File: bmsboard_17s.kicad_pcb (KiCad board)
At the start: 2 copper layers, 141 parts, among them Q1 Q_NMOS_GDS, Q10 Q_NMOS_GDS, Q11 Q_NMOS_GDS, Q12 Q_PMOS_GDS, Q13 Q_NMOS_GDS, Q14 Q_NMOS_GDS, Q15 Q_NMOS_GDS, Q16 Q_NMOS_GDS, Q17 Q_NMOS_GDS, Q18 Q_NMOS_GDS, Q19 Q_NMOS_GDS, Q2 Q_NMOS_GDS, Q20 Q_NMOS_GDS, Q21 Q_NPN_BCE, Q3 Q_NMOS_GDS, Q4 Q_NMOS_GDS, Q5 Q_NMOS_GDS, Q6 Q_NMOS_GDS, Q7 Q_NMOS_GDS, Q8 Q_NMOS_GDS, Q9 Q_NMOS_GDS, U1 PB7170

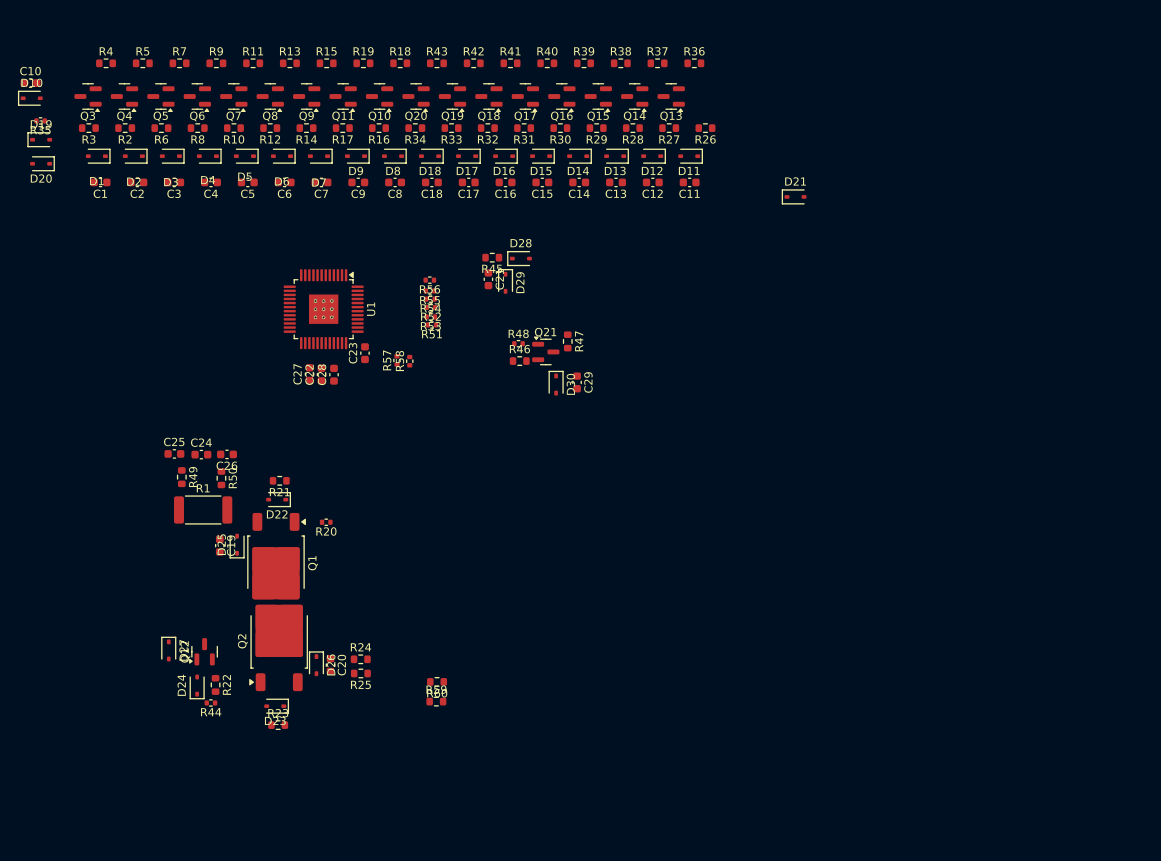
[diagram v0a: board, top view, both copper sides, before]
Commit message: 重新分配位号，使电压采样电路的位号连续
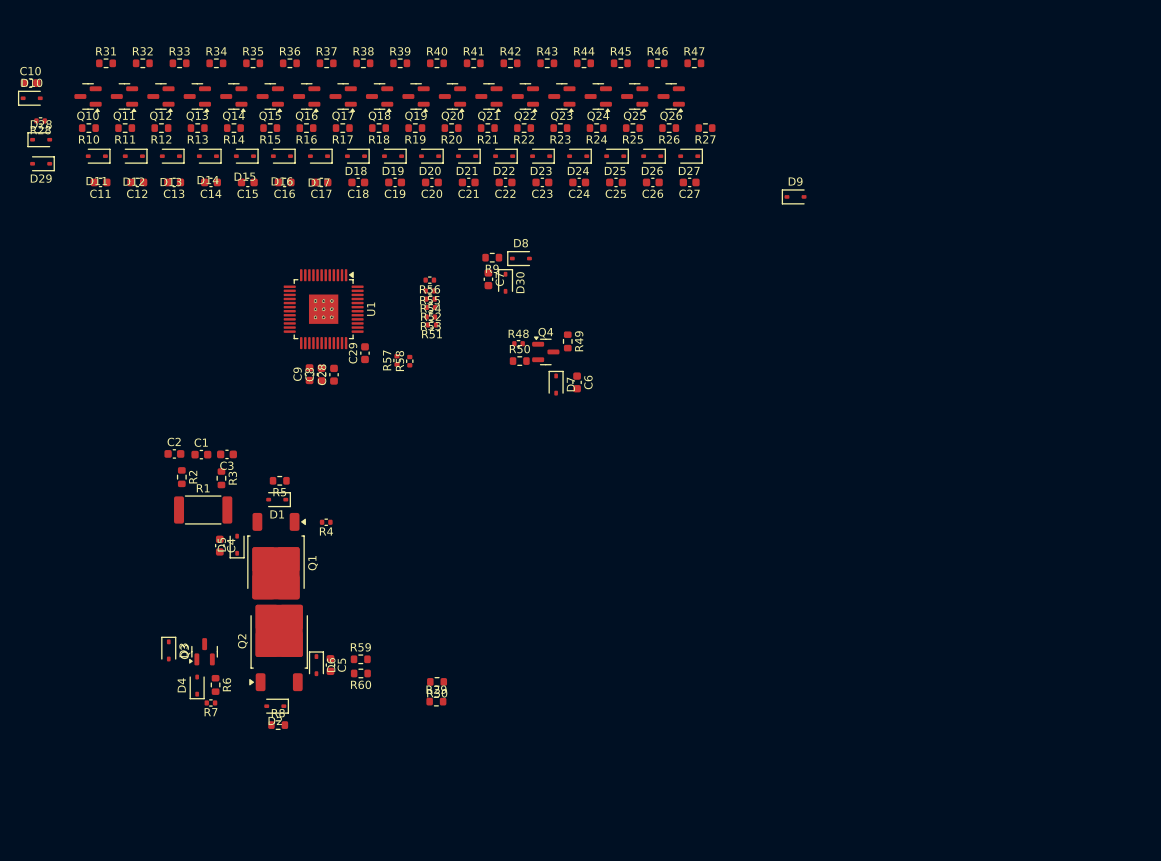
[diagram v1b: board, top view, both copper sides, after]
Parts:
- renumbered C24 to C1, C1 to C11, C2 to C12, C3 to C13, C4 to C14, C5 to C15, C6 to C16, C7 to C17, C9 to C18, C8 to C19, C25 to C2, C18 to C20, C17 to C21, C16 to C22, C15 to C23, C14 to C24, C13 to C25, C12 to C26, C11 to C27, C23 to C29, C26 to C3, C19 to C4, C20 to C5, C29 to C6, C21 to C7, C22 to C8, C27 to C9, D22 to D1, D1 to D11, D2 to D12, D3 to D13, D4 to D14, D5 to D15, D6 to D16, D7 to D17, D9 to D18, D8 to D19, D23 to D2, D18 to D20, D17 to D21, D16 to D22, D15 to D23, D14 to D24, D13 to D25, D12 to D26, D11 to D27, D19 to D28, D20 to D29, D27 to D3, D29 to D30, D24 to D4, D25 to D5, D26 to D6, D30 to D7, D28 to D8, D21 to D9, Q3 to Q10, Q4 to Q11, Q5 to Q12, Q6 to Q13, Q7 to Q14, Q8 to Q15, Q9 to Q16, Q11 to Q17, Q10 to Q18, Q20 to Q19, Q19 to Q20, Q18 to Q21, Q17 to Q22, Q16 to Q23, Q15 to Q24, Q14 to Q25, Q13 to Q26, Q12 to Q3, Q21 to Q4, R3 to R10, R2 to R11, R6 to R12, R8 to R13, R10 to R14, R12 to R15, R14 to R16, R16 to R18, R34 to R19, R49 to R2, R33 to R20, R32 to R21, R31 to R22, R30 to R23, R29 to R24, R28 to R25, R27 to R26, R26 to R27, R35 to R28, R59 to R29, R50 to R3, R60 to R30, R4 to R31, R5 to R32, R7 to R33, R9 to R34, R11 to R35, R13 to R36, R15 to R37, R19 to R38, R18 to R39, R20 to R4, R43 to R40, R42 to R41, R41 to R42, R40 to R43, R39 to R44, R38 to R45, R37 to R46, R36 to R47, R47 to R49, R21 to R5, R46 to R50, R24 to R59, R22 to R6, R25 to R60, R44 to R7, R23 to R8, R45 to R9

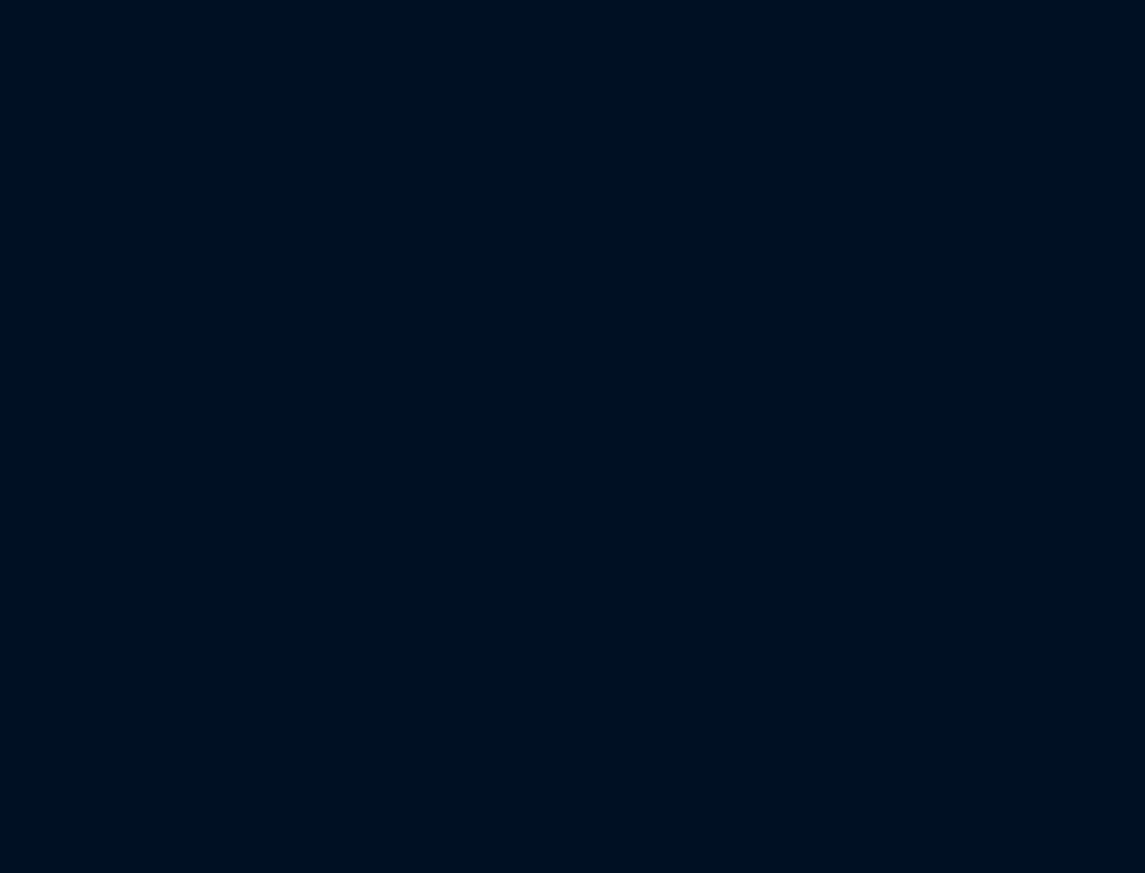
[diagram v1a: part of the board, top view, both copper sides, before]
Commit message: fix: 修复commit `38e8c9e`将元器件移动子原理图到造成的位号混乱
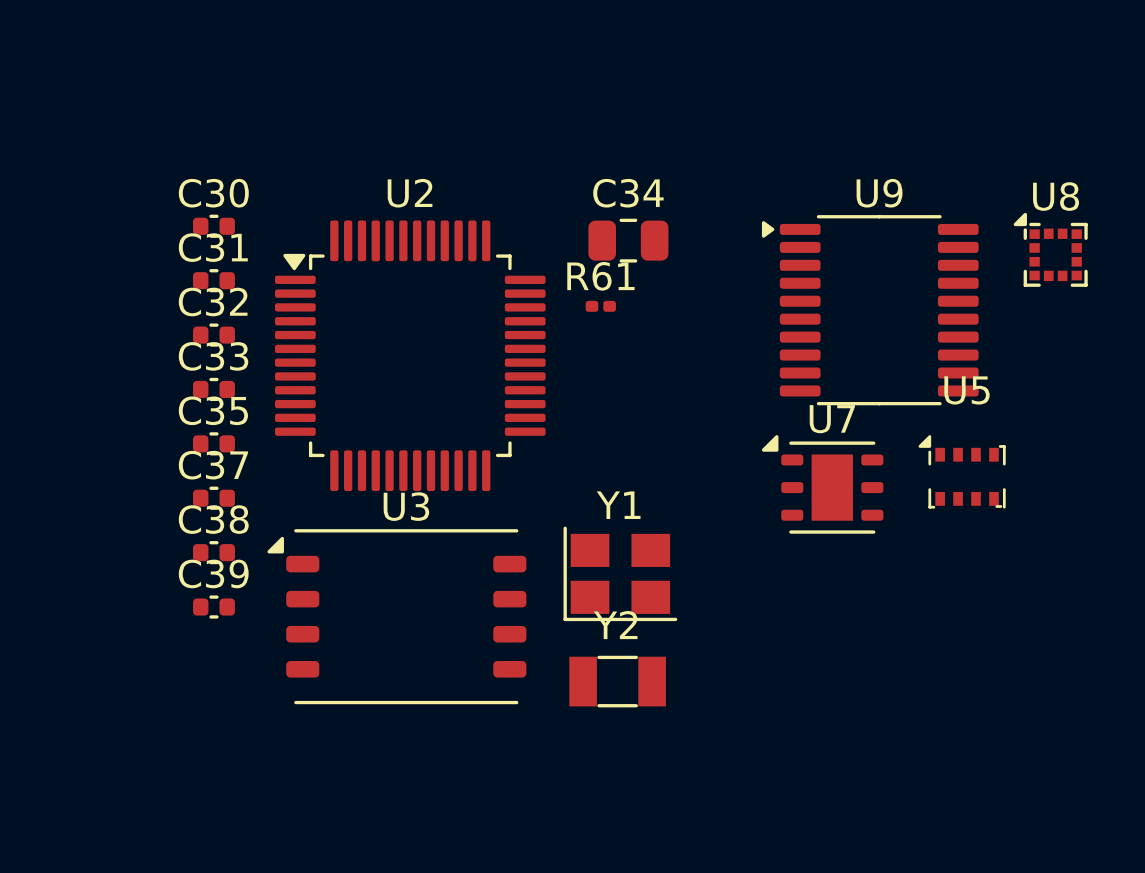
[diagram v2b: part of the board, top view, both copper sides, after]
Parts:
- added C30: 8p, Capacitor_SMD:C_0402_1005Metric, F.Cu at (122.4, 76.6)
- added C31: 8p, Capacitor_SMD:C_0402_1005Metric, F.Cu at (122.4, 78.6)
- added C32: 12.5p, Capacitor_SMD:C_0402_1005Metric, F.Cu at (122.4, 80.6)
- added C33: 12.5p, Capacitor_SMD:C_0402_1005Metric, F.Cu at (122.4, 82.5)
- added C34: 22u, Capacitor_SMD:C_0805_2012Metric, F.Cu at (137.4, 77.1)
- added C35: 100n, Capacitor_SMD:C_0402_1005Metric, F.Cu at (122.4, 84.5)
- added C37: 100n, Capacitor_SMD:C_0402_1005Metric, F.Cu at (122.4, 86.5)
- added C38: 100n, Capacitor_SMD:C_0402_1005Metric, F.Cu at (122.4, 88.4)
- added C39: 100n, Capacitor_SMD:C_0402_1005Metric, F.Cu at (122.4, 90.4)
- added R61: 10k, Resistor_SMD:R_0201_0603Metric, F.Cu at (136.4, 79.5)
- added U2: CH32V103C8T6, Package_QFP:LQFP-48_7x7mm_P0.5mm, F.Cu at (129.5, 81.3)
- added U3: XTSD01G, Package_LGA:LGA-8_8x6mm_P1.27mm, F.Cu at (129.4, 90.8)
- added U5: BMP280, Package_LGA:Bosch_LGA-8_2x2.5mm_P0.65mm_ClockwisePinNumbering, F.Cu at (149.7, 85.7)
- added U7: Si7020-A20, Package_DFN_QFN:DFN-6-1EP_3x3mm_P1mm_EP1.5x2.4mm, F.Cu at (144.8, 86.1)
- added U8: QMA6100P, Package_LGA:LGA-12_2x2mm_P0.5mm, F.Cu at (152.9, 77.7)
- added U9: ADS1243, Package_SO:TSSOP-20_4.4x6.5mm_P0.65mm, F.Cu at (146.5, 79.7)
- added Y1: 16MHz, Crystal:Crystal_SMD_3225-4Pin_3.2x2.5mm, F.Cu at (137.1, 89.2)
- added Y2: 32.768kHz, Crystal:Crystal_SMD_3215-2Pin_3.2x1.5mm, F.Cu at (137.0, 93.1)
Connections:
- net /ALERT renamed /AFE Module/ALERT
- net /BAT+ renamed /AFE Module/BAT+
- net /BAT- renamed /AFE Module/BAT-
- net /BAT0 renamed /AFE Module/BAT0
- net /BAT1 renamed /AFE Module/BAT1
- net /BAT10 renamed /AFE Module/BAT10
- net /BAT11 renamed /AFE Module/BAT11
- net /BAT12 renamed /AFE Module/BAT12
- net /BAT13 renamed /AFE Module/BAT13
- net /BAT14 renamed /AFE Module/BAT14
- net /BAT15 renamed /AFE Module/BAT15
- net /BAT16 renamed /AFE Module/BAT16
- net /BAT17 renamed /AFE Module/BAT17
- net /BAT2 renamed /AFE Module/BAT2
- net /BAT3 renamed /AFE Module/BAT3
- net /BAT4 renamed /AFE Module/BAT4
- net /BAT5 renamed /AFE Module/BAT5
- net /BAT6 renamed /AFE Module/BAT6
- net /BAT7 renamed /AFE Module/BAT7
- net /BAT8 renamed /AFE Module/BAT8
- net /BAT9 renamed /AFE Module/BAT9
- net /C0 renamed /AFE Module/C0
- net /C1 renamed /AFE Module/C1
- net /C10 renamed /AFE Module/C10
- net /C11 renamed /AFE Module/C11
- net /C12 renamed /AFE Module/C12
- net /C13 renamed /AFE Module/C13
- net /C14 renamed /AFE Module/C14
- net /C15 renamed /AFE Module/C15
- net /C16 renamed /AFE Module/C16
- net /C17 renamed /AFE Module/C17
- net /C2 renamed /AFE Module/C2
- net /C3 renamed /AFE Module/C3
- net /C4 renamed /AFE Module/C4
- net /C5 renamed /AFE Module/C5
- net /C6 renamed /AFE Module/C6
- net /C7 renamed /AFE Module/C7
- net /C8 renamed /AFE Module/C8
- net /C9 renamed /AFE Module/C9
- net /CHG renamed /AFE Module/CHG
- net /CHGD renamed /AFE Module/CHGD
- net /CS_AFE renamed /AFE Module/CS_AFE
- net /DRIVE renamed /AFE Module/DRIVE
- net /DSG renamed /AFE Module/DSG
- net /GPIO1 renamed /AFE Module/GPIO1
- net /GPIO2 renamed /AFE Module/GPIO2
- net /LODD renamed /AFE Module/LODD
- net /MISO renamed /AFE Module/MISO
- net /MOSI renamed /AFE Module/MOSI
- net /PACK- renamed /AFE Module/PACK-
- net /SCLK renamed /AFE Module/SCLK
- net /SRN renamed /AFE Module/SRN
- net /SRP renamed /AFE Module/SRP

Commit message: 添加PB7170(LQFP-64)符号，原符号重命名为PB7170P48(LQFP-48)并应用于原理图，更新到PCB文件
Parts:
- added U10: TJA1042T-3, Package_SO:SOIC-8_3.9x4.9mm_P1.27mm, F.Cu at (132.2, 68.8)
- U1: value PB7170 -> PB7170P48; footprint Package_QFP:LQFP-48-1EP_7x7mm_P0.5mm_EP3.6x3.6mm_ThermalVias -> Package_QFP:LQFP-48_7x7mm_P0.5mm
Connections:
- U2 pad 10: unconnected-(U2-PA0-Pad10) -> /MCU Module/KEY_WKUP
- U2 pad 11: unconnected-(U2-PA1-Pad11) -> /RTEMP_OUT0
- U2 pad 12: unconnected-(U2-PA2-Pad12) -> /RTEMP_OUT1
- U2 pad 13: unconnected-(U2-PA3-Pad13) -> /RTEMP_OUT2
- U2 pad 14: unconnected-(U2-PA4-Pad14) -> /RTEMP_OUT3
- U2 pad 15: unconnected-(U2-PA5-Pad15) -> /WDET_OUT
- U2 pad 16: unconnected-(U2-PA6-Pad16) -> /MCU Module/LED_R
- U2 pad 17: unconnected-(U2-PA7-Pad17) -> /MCU Module/LED_G
- U2 pad 18: unconnected-(U2-PB0-Pad18) -> /MCU Module/LED_B
- U2 pad 19: unconnected-(U2-PB1-Pad19) -> /WDET_PWM
- U2 pad 20: unconnected-(U2-PB2-Pad20) -> /WDET_EN
- U2 pad 21: unconnected-(U2-PB10-Pad21) -> /MCU Module/SCL2
- U2 pad 22: unconnected-(U2-PB11-Pad22) -> /MCU Module/SDA2
- U2 pad 25: unconnected-(U2-PB12-Pad25) -> /RTEMP_R0
- U2 pad 26: unconnected-(U2-PB13-Pad26) -> /RTEMP_R1
- U2 pad 27: unconnected-(U2-PB14-Pad27) -> /RTEMP_R2
- U2 pad 28: unconnected-(U2-PB15-Pad28) -> /RTEMP_EN
- U2 pad 29: unconnected-(U2-PA8-Pad29) -> /CS_AD
- U2 pad 30: unconnected-(U2-PA9-Pad30) -> /MCU Module/TXD1
- U2 pad 31: unconnected-(U2-PA10-Pad31) -> /MCU Module/RXD1
- U2 pad 32: unconnected-(U2-PA11-Pad32) -> /MCU Module/CANRX
- U2 pad 33: unconnected-(U2-PA12-Pad33) -> /MCU Module/CANTX
- U2 pad 34: unconnected-(U2-PA13-Pad34) -> /MCU Module/CANSTB
- U2 pad 37: unconnected-(U2-PA14-Pad37) -> /CS_AFE
- U2 pad 38: unconnected-(U2-PA15-Pad38) -> /CS_BLE
- U2 pad 39: unconnected-(U2-PB3-Pad39) -> /SCLK
- U2 pad 40: unconnected-(U2-PB4-Pad40) -> /MISO
- U2 pad 41: unconnected-(U2-PB5-Pad41) -> /MOSI
- U2 pad 42: unconnected-(U2-PB6-Pad42) -> /SCL1
- U2 pad 43: unconnected-(U2-PB7-Pad43) -> /SDA1
- U2 pad 45: unconnected-(U2-PB8-Pad45) -> /MCU Module/SPK+
- U2 pad 46: unconnected-(U2-PB9-Pad46) -> /MCU Module/SPK-
- U5 pad 3: /Sensors Module/SDA -> /SDA1
- U5 pad 4: /Sensors Module/SCL -> /SCL1
- U7 pad 1: /Sensors Module/SDA -> /SDA1
- U7 pad 6: /Sensors Module/SCL -> /SCL1
- U9 pad 16: /Sensors Module/CS_AD -> /CS_AD
- U9 pad 17: /Sensors Module/MOSI -> /MOSI
- U9 pad 18: /Sensors Module/MISO -> /MISO
- U9 pad 19: /Sensors Module/SCLK -> /SCLK
